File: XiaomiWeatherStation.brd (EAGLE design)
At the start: 70 x 100 mm, 12 parts, among them K1 RELAY-SPDT, Q1 BD437

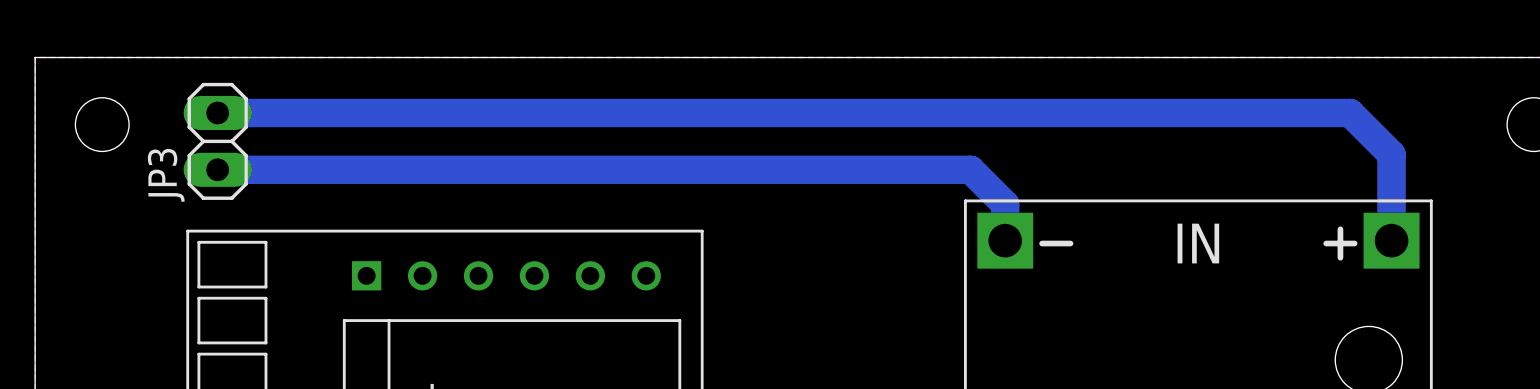
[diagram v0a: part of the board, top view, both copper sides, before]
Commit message: adds 3d models
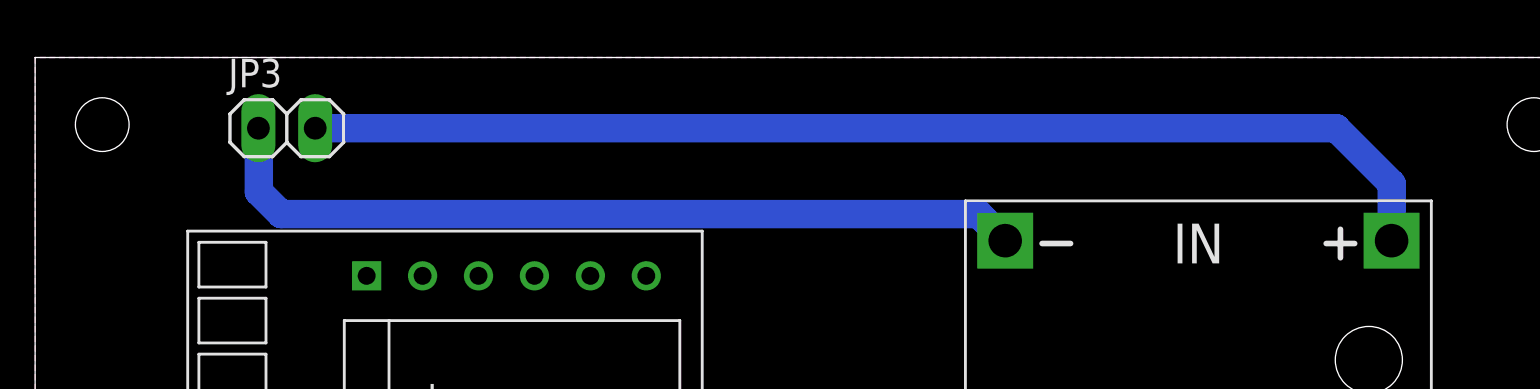
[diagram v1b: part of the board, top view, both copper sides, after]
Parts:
- moved JP3 3.15 mm to (11.2, 96.8), turned to 0 degrees
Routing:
- net IN+: track 57.1 -> 51.7 mm
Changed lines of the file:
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@@
 </layers>
 <board>
-<fusionsync huburn="a.cGVyc29uYWw6dWUyYzhmNzA4" projecturn="a.cGVyc29uYWw6dWUyYzhmNzA4IzIwMTkwMTMwMTczMjM4ODgx" f3durn="urn:adsk.wipprod:dm.lineage:spPOfCMSSPOzXMC2o5ZuhA" pcbguid="" lastpulledtime="" lastsyncedchangeguid="" latestrevisionid="b0fe3381-a17d-4749-aa34-8e1b42c0f3a5" lastsyncedrevisionid="b0fe3381-a17d-4749-aa34-8e1b42c0f3a5" lastboardhashguid="bfa94db5-b19a-87e9-10ab-6378246ddbf7" lastpushedtime="2021-10-17T12:46:15Z" linktopcb3d="true"/>
+<fusionsync huburn="a.cGVyc29uYWw6dWUyYzhmNzA4" projecturn="a.cGVyc29uYWw6dWUyYzhmNzA4IzIwMTkwMTMwMTczMjM4ODgx" f3durn="urn:adsk.wipprod:dm.lineage:spPOfCMSSPOzXMC2o5ZuhA" pcbguid="" lastpulledtime="" lastsyncedchangeguid="" latestrevisionid="199a9939-6ca1-449c-8d37-db30be5e7dd4" lastsyncedrevisionid="199a9939-6ca1-449c-8d37-db30be5e7dd4" lastboardhashguid="cdd145cb-bfe3-e544-9fc3-301cddd6bfee" lastpushedtime="2021-11-08T18:51:43Z" linktopcb3d="true"/>
 <plain>
 <wire x1="0" y1="0" x2="70" y2="0" width="0" layer="20"/>
@@
 <attribute name="VALUE" x="40.57" y="72" size="1.27" layer="27" rot="R270" align="top-center"/>
 </element>
-<element name="JP3" library="pinhead" library_urn="urn:adsk.eagle:library:325" package="1X02" package3d_urn="urn:adsk.eagle:package:22435/2" value="" x="8.16" y="96.25" smashed="yes" rot="R90">
-<attribute name="NAME" x="6.3312" y="93.6338" size="1.27" layer="25" ratio="10" rot="R90"/>
-<attribute name="POPULARITY" value="98" x="8.16" y="96.25" size="1.778" layer="27" rot="R90" display="off"/>
-<attribute name="VALUE" x="11.335" y="93.71" size="1.27" layer="27" rot="R90"/>
+<element name="JP3" library="pinhead" library_urn="urn:adsk.eagle:library:325" package="1X02" package3d_urn="urn:adsk.eagle:package:22435/2" value="" x="11.25" y="96.84" smashed="yes">
+<attribute name="NAME" x="8.6338" y="98.6688" size="1.27" layer="25" ratio="10"/>
+<attribute name="POPULARITY" value="98" x="11.25" y="96.84" size="1.778" layer="27" display="off"/>
+<attribute name="VALUE" x="8.71" y="93.665" size="1.27" layer="27"/>
 </element>
 <element name="R1" library="rcl" library_urn="urn:adsk.eagle:library:334" package="0204/7" package3d_urn="urn:adsk.eagle:package:23498/2" value="1k" x="37" y="10" smashed="yes" rot="R90">
@@
 <attribute name="VALUE" x="40.36" y="4.463" size="1.778" layer="27" ratio="10" rot="R90"/>
 </element>
-<element name="J1" library="SparkFun-Connectors" library_urn="urn:adsk.eagle:library:31567038" package="SCREWTERMINAL-5MM-2" package3d_urn="urn:adsk.eagle:package:31567599/1" value="" x="59.9" y="6.8" smashed="yes" rot="R180">
+<element name="J1" library="SparkFun-Connectors" library_urn="urn:adsk.eagle:library:31567038" package="SCREWTERMINAL-5MM-2" package3d_urn="urn:adsk.eagle:package:31567599/2" value="" x="59.9" y="6.8" smashed="yes" rot="R180">
 <attribute name="NAME" x="61.17" y="4.26" size="0.6096" layer="25" font="vector" ratio="20" rot="R180"/>
 <attribute name="SF_SKU" value="PRT-08432" x="59.9" y="6.8" size="1.778" layer="27" rot="R180" display="off"/>
@@
 <contactref element="U$3" pad="IN-"/>
 <contactref element="JP3" pad="1"/>
-<wire x1="8.16" y1="94.98" x2="41.82" y2="94.98" width="1.27" layer="16"/>
-<wire x1="43.364" y1="93.436" x2="43.364" y2="91.812" width="1.27" layer="16"/>
-<wire x1="41.82" y1="94.98" x2="43.364" y2="93.436" width="1.27" layer="16"/>
+<wire x1="9.98" y1="96.84" x2="10" y2="96.82" width="1.27" layer="16"/>
+<wire x1="10" y1="96.82" x2="10" y2="94" width="1.27" layer="16"/>
+<wire x1="10" y1="94" x2="11" y2="93" width="1.27" layer="16"/>
+<wire x1="42.176" y1="93" x2="43.364" y2="91.812" width="1.27" layer="16"/>
+<wire x1="11" y1="93" x2="42.176" y2="93" width="1.27" layer="16"/>
 </signal>
 <signal name="3V7">
@@
 <contactref element="JP3" pad="2"/>
 <contactref element="U$3" pad="IN+"/>
-<wire x1="8.16" y1="97.52" x2="58.78" y2="97.52" width="1.27" layer="16"/>
-<wire x1="60.636" y1="95.664" x2="60.636" y2="91.812" width="1.27" layer="16"/>
-<wire x1="58.78" y1="97.52" x2="60.636" y2="95.664" width="1.27" layer="16"/>
+<wire x1="12.52" y1="96.84" x2="58.16" y2="96.84" width="1.27" layer="16"/>
+<wire x1="60.636" y1="94.364" x2="60.636" y2="91.812" width="1.27" layer="16"/>
+<wire x1="58.16" y1="96.84" x2="60.636" y2="94.364" width="1.27" layer="16"/>
 </signal>
 <signal name="COLLECTOR">
